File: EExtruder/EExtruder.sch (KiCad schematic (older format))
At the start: 40 parts, among them J1 20A 50V, J11 Conn_01x03_Male, J2 AudioJack4_Ground, U1 STM32F030C8Tx, U2 DCBuck, Y1 8MHz

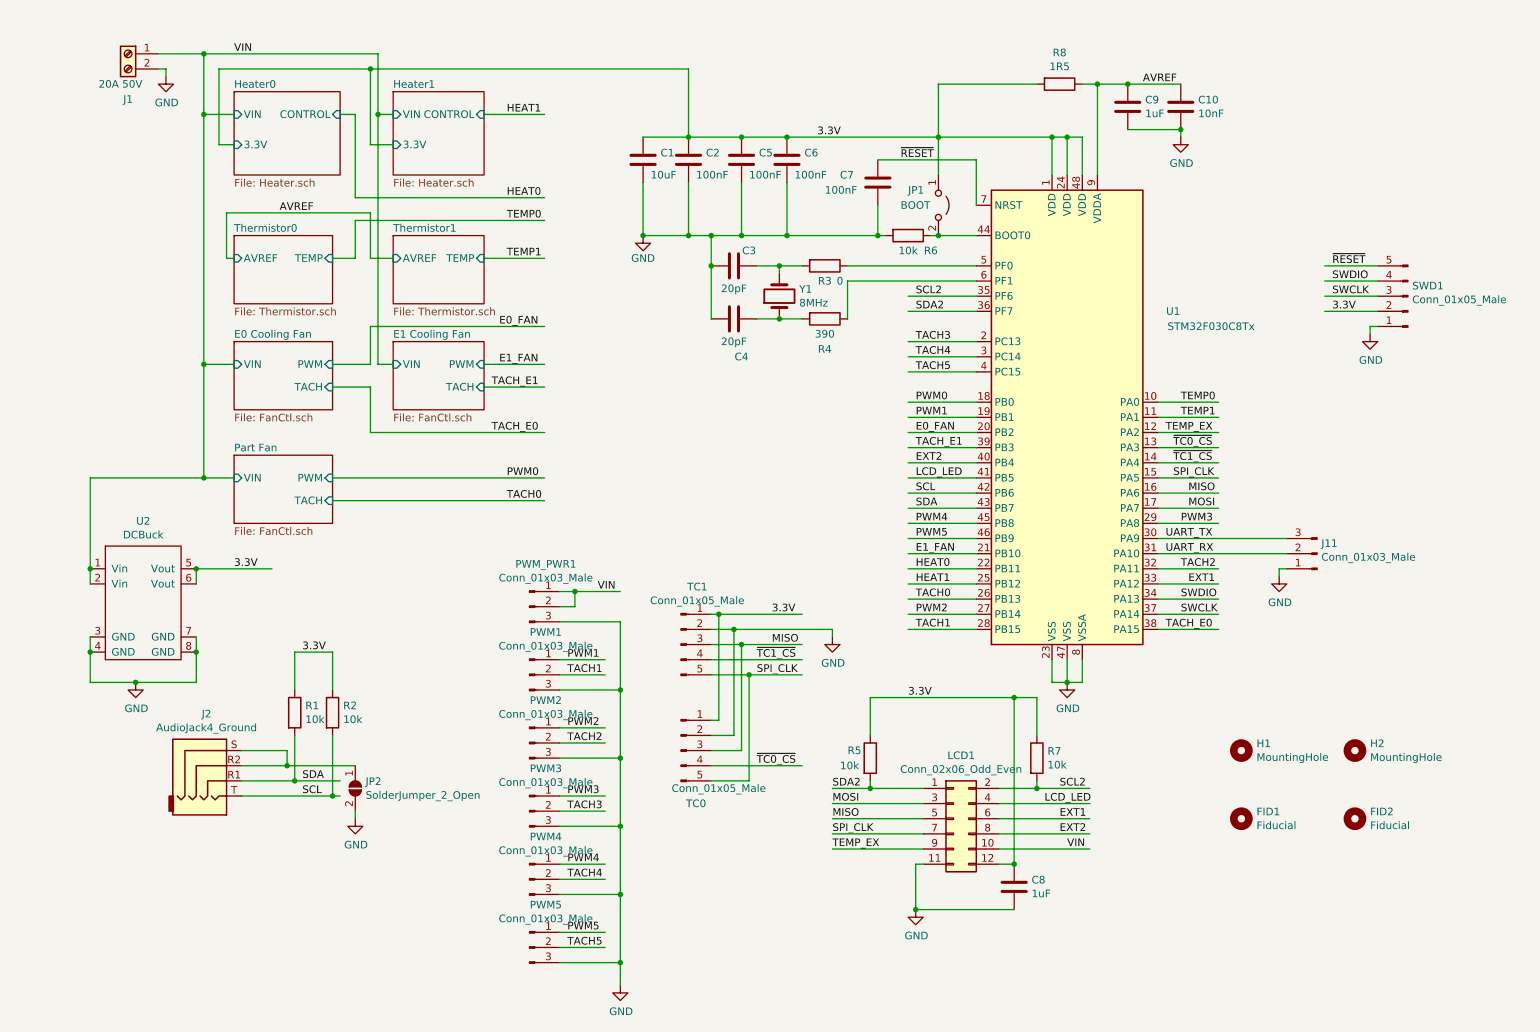
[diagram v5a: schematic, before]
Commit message: Added 3.3V LDO, updated TC connectors to 6 pins. Re-arranged the layout.
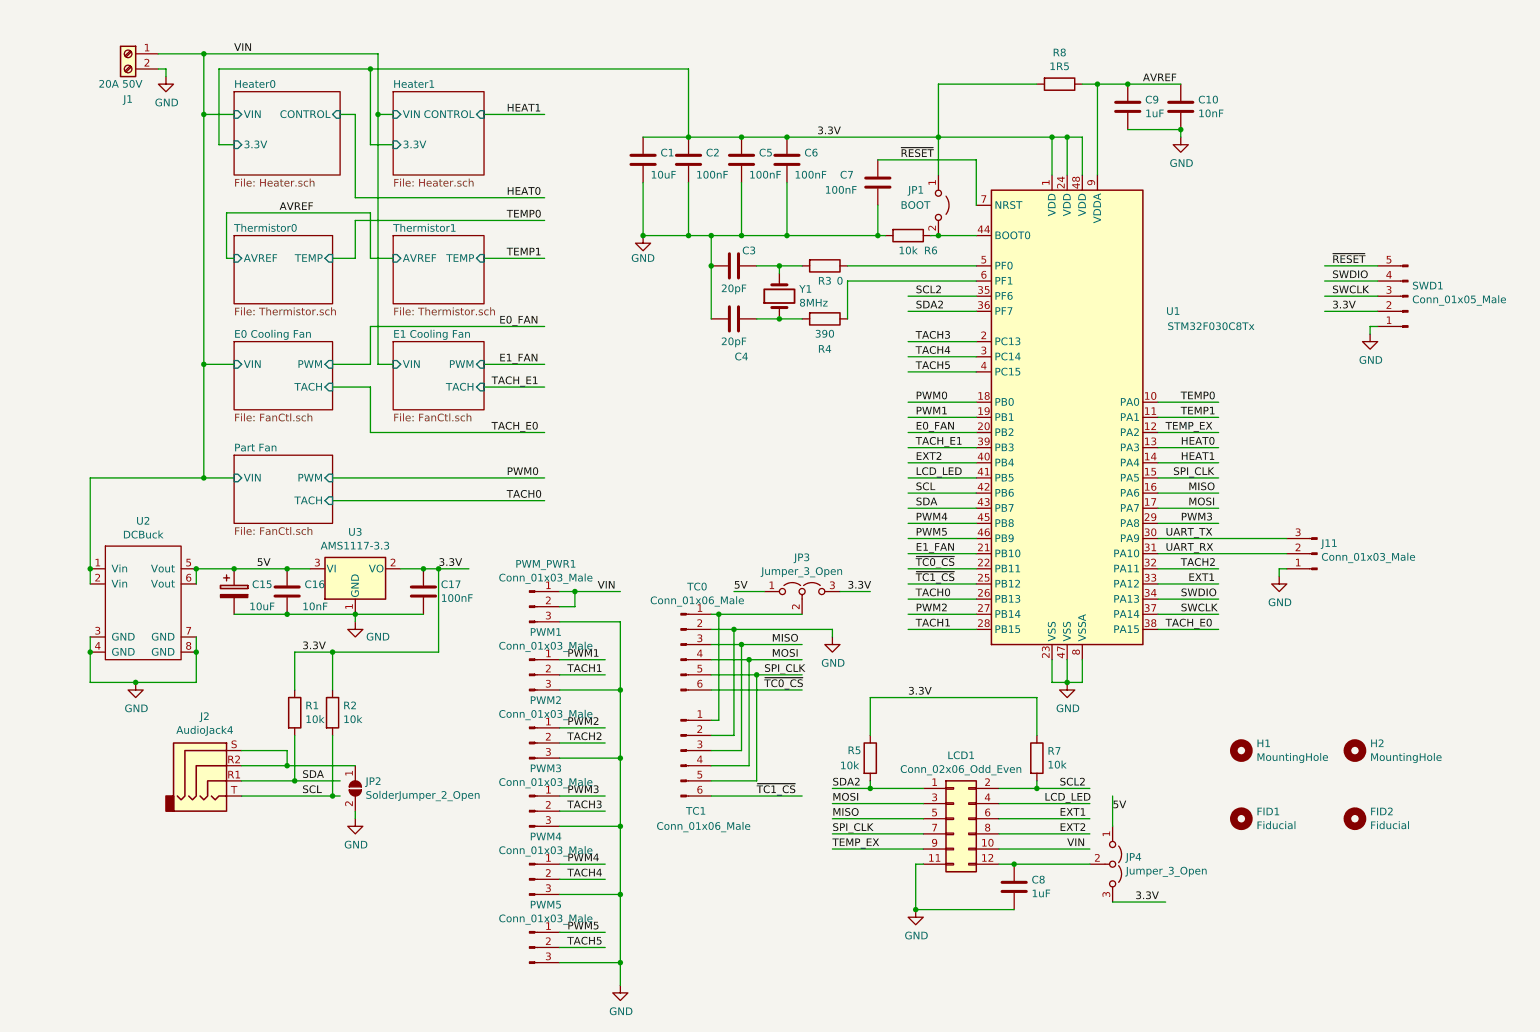
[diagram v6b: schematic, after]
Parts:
- removed J2: AudioJack4_Ground, PJ320D:Jack_3.5mm_PJ320D_Horizontal, symbol Connector:AudioJack4_Ground
- removed TC0, TC1: Conn_01x05_Male, Connector_PinHeader_2.54mm:PinHeader_1x05_P2.54mm_Vertical, symbol Connector:Conn_01x05_Male
- added C15: 10uF, Local:C_0603_1608Metric, symbol Device:CP
- added C16: 10nF, Local:C_0603_1608Metric, symbol Device:C
- added C17: 100nF, Local:C_0603_1608Metric, symbol Device:C
- added J2: AudioJack4, PJ320D:Jack_3.5mm_PJ320D_Horizontal, symbol Connector:AudioJack4
- added JP3, JP4: Jumper_3_Open, Jumper:SolderJumper-3_P1.3mm_Open_Pad1.0x1.5mm, symbol Jumper:Jumper_3_Open
- added TC0, TC1: Conn_01x06_Male, Connector_PinHeader_2.54mm:PinHeader_1x06_P2.54mm_Vertical, symbol Connector:Conn_01x06_Male
- added U3: AMS1117-3.3, Package_TO_SOT_SMD:SOT-223-3_TabPin2, symbol Regulator_Linear:AMS1117-3.3
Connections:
- net labels added: 5V
- wire segments 231 -> 249
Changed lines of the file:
@@
 EESchema Schematic File Version 4
 LIBS:EExtruder-cache
-EELAYER 28 0
+EELAYER 29 0
 EELAYER END
 $Descr A4 11693 8268
@@
 Text Label 8200 3350 0    50   ~ 0
 TEMP_EX
-Text Label 8250 3450 0    50   ~ 0
-~TC0_CS
-Text Label 8250 3550 0    50   ~ 0
-~TC1_CS
 Text Label 8250 3650 0    50   ~ 0
 SPI_CLK
@@
 Text Label 6550 4150 0    50   ~ 0
 E1_FAN
-Text Label 6550 4250 0    50   ~ 0
-HEAT0
-Text Label 6550 4350 0    50   ~ 0
-HEAT1
 Text Label 6550 4450 0    50   ~ 0
 TACH0
@@
 Text Label 2050 850  0    50   ~ 0
 VIN
-$Comp
-L Connector:Conn_01x05_Male TC1
-U 1 1 5BEB14A1
-P 5000 4750
-F 0 "TC1" H 5108 5131 50  0000 C CNN
-F 1 "Conn_01x05_Male" H 5108 5040 50  0000 C CNN
-F 2 "Connector_PinHeader_2.54mm:PinHeader_1x05_P2.54mm_Vertical" H 5000 4750 50  0001 C CNN
-F 3 "~" H 5000 4750 50  0001 C CNN
-	1    5000 4750
-	1    0    0    -1
-$EndComp
-$Comp
-L Connector:Conn_01x05_Male TC0
-U 1 1 5BEB5291
-P 5000 5450
-F 0 "TC0" H 5100 5100 50  0000 C CNN
-F 1 "Conn_01x05_Male" H 5250 5200 50  0000 C CNN
-F 2 "Connector_PinHeader_2.54mm:PinHeader_1x05_P2.54mm_Vertical" H 5000 5450 50  0001 C CNN
-F 3 "~" H 5000 5450 50  0001 C CNN
-	1    5000 5450
-	1    0    0    -1
-$EndComp
-Wire Wire Line
-	5200 5550 5800 5550
-Wire Wire Line
-	5200 4950 5450 4950
 Wire Wire Line
 	5200 4550 5250 4550
@@
 	5200 4750 5400 4750
 Wire Wire Line
-	5200 4850 5800 4850
-Text Label 5600 4550 0    50   ~ 0
-3.3V
+	5200 4850 5450 4850
 Text Label 5600 4750 0    50   ~ 0
 MISO
-Text Label 5500 4850 0    50   ~ 0
-~TC1_CS
-Text Label 5500 4950 0    50   ~ 0
+Text Label 5550 4950 0    50   ~ 0
 SPI_CLK
-Text Label 5500 5550 0    50   ~ 0
-~TC0_CS
-Wire Wire Line
-	5200 5650 5450 5650
-Wire Wire Line
-	5450 5650 5450 4950
-Connection ~ 5450 4950
-Wire Wire Line
-	5450 4950 5800 4950
 Wire Wire Line
 	5200 5450 5400 5450
@@
 	7350 5350 7350 5100
 Wire Wire Line
-	7350 5100 7200 5100
-Wire Wire Line
 	6250 5100 6250 5350
 Text Label 6500 5100 0    50   ~ 0
@@
 Wire Wire Line
 	7100 6000 7700 6000
-Connection ~ 7200 5100
-Wire Wire Line
-	7200 5100 6250 5100
 $Comp
 L power:GND #PWR06
@@
 	7100 6200 7200 6200
 Wire Wire Line
-	7200 5100 7200 6200
-Connection ~ 7200 6200
-Wire Wire Line
 	7200 6500 6550 6500
 Connection ~ 6550 6500
@@
 Connection ~ 1850 3650
 Wire Wire Line
-	1800 4250 2300 4250
-Text Label 2050 4250 0    50   ~ 0
-3.3V
-Wire Wire Line
 	1800 4800 1800 5000
-$Comp
-L Connector:AudioJack4_Ground J2
-U 1 1 5C23C3B0
-P 1900 5550
-F 0 "J2" H 1868 5892 50  0000 C CNN
-F 1 "AudioJack4_Ground" H 1868 5801 50  0000 C CNN
-F 2 "PJ320D:Jack_3.5mm_PJ320D_Horizontal" H 1900 5550 50  0001 C CNN
-F 3 "~" H 1900 5550 50  0001 C CNN
-	1    1900 5550
-	1    0    0    -1
-$EndComp
 $Comp
 L BuckConverter:DCBuck U2
@@
 	1    0    0    -1
 $EndComp
+$Comp
+L Connector:Conn_01x06_Male TC0
+U 1 1 5C3BD554
+P 5000 4750
+F 0 "TC0" H 5108 5131 50  0000 C CNN
+F 1 "Conn_01x06_Male" H 5108 5040 50  0000 C CNN
+F 2 "Connector_PinHeader_2.54mm:PinHeader_1x06_P2.54mm_Vertical" H 5000 4750 50  0001 C CNN
+F 3 "~" H 5000 4750 50  0001 C CNN
+	1    5000 4750
+	1    0    0    -1
+$EndComp
+$Comp
+L Connector:Conn_01x06_Male TC1
+U 1 1 5C3BE824
+P 5000 5450
+F 0 "TC1" H 5100 5050 50  0000 C CNN
+F 1 "Conn_01x06_Male" H 5150 4950 50  0000 C CNN
+F 2 "Connector_PinHeader_2.54mm:PinHeader_1x06_P2.54mm_Vertical" H 5000 5450 50  0001 C CNN
+F 3 "~" H 5000 5450 50  0001 C CNN
+	1    5000 5450
+	1    0    0    -1
+$EndComp
+Wire Wire Line
+	5200 4950 5500 4950
+Wire Wire Line
+	5200 5550 5450 5550
+Wire Wire Line
+	5450 5550 5450 4850
+Connection ~ 5450 4850
+Wire Wire Line
+	5450 4850 5800 4850
+Wire Wire Line
+	5500 5650 5500 4950
+Wire Wire Line
+	5200 5650 5500 5650
+Connection ~ 5500 4950
+Wire Wire Line
+	5500 4950 5800 4950
+Text Label 5600 4850 0    50   ~ 0
+MOSI
+Wire Wire Line
+	5200 5050 5800 5050
+Wire Wire Line
+	5200 5750 5800 5750
+Text Label 5500 5750 0    50   ~ 0
+~TC1_CS
+Text Label 5550 5050 0    50   ~ 0
+~TC0_CS
+$Comp
+L Regulator_Linear:AMS1117-3.3 U3
+U 1 1 5C40648A
+P 2850 4250
+F 0 "U3" H 2850 4492 50  0000 C CNN
+F 1 "AMS1117-3.3" H 2850 4401 50  0000 C CNN
+F 2 "Package_TO_SOT_SMD:SOT-223-3_TabPin2" H 2850 4450 50  0001 C CNN
+F 3 "http://www.advanced-monolithic.com/pdf/ds1117.pdf" H 2950 4000 50  0001 C CNN
+	1    2850 4250
+	1    0    0    -1
+$EndComp
+Wire Wire Line
+	3150 4250 3300 4250
+Text Label 3400 4250 0    50   ~ 0
+3.3V
+$Comp
+L power:GND #PWR018
+U 1 1 5C41A303
+P 2850 4600
+F 0 "#PWR018" H 2850 4350 50  0001 C CNN
+F 1 "GND" H 3000 4500 50  0000 C CNN
+F 2 "" H 2850 4600 50  0001 C CNN
+F 3 "" H 2850 4600 50  0001 C CNN
+	1    2850 4600
+	1    0    0    -1
+$EndComp
+Wire Wire Line
+	2850 4600 2850 4550
+Wire Wire Line
+	1800 4250 2050 4250
+$Comp
+L Device:CP C15
+U 1 1 5C43F401
+P 2050 4400
+F 0 "C15" H 2168 4446 50  0000 L CNN
+F 1 "10uF" H 2150 4300 50  0000 L CNN
+F 2 "Local:C_0603_1608Metric" H 2088 4250 50  0001 C CNN
+F 3 "~" H 2050 4400 50  0001 C CNN
+	1    2050 4400
+	1    0    0    -1
+$EndComp
+Connection ~ 2050 4250
+Wire Wire Line
+	2050 4250 2400 4250
+$Comp
+L Device:C C16
+U 1 1 5C440037
+P 2400 4400
+F 0 "C16" H 2515 4446 50  0000 L CNN
+F 1 "10nF" H 2500 4300 50  0000 L CNN
+F 2 "Local:C_0603_1608Metric" H 2438 4250 50  0001 C CNN
+F 3 "~" H 2400 4400 50  0001 C CNN
+	1    2400 4400
+	1    0    0    -1
+$EndComp
+Connection ~ 2400 4250
+Wire Wire Line
+	2400 4250 2550 4250
+$Comp
+L Device:C C17
+U 1 1 5C4407B0
+P 3300 4400
+F 0 "C17" H 3415 4446 50  0000 L CNN
+F 1 "100nF" H 3415 4355 50  0000 L CNN
+F 2 "Local:C_0603_1608Metric" H 3338 4250 50  0001 C CNN
+F 3 "~" H 3300 4400 50  0001 C CNN
+	1    3300 4400
+	1    0    0    -1
+$EndComp
+Connection ~ 3300 4250
+Wire Wire Line
+	3300 4250 3400 4250
+Wire Wire Line
+	2050 4550 2400 4550
+Connection ~ 2850 4550
+Connection ~ 2400 4550
+Wire Wire Line
+	2400 4550 2850 4550
+Wire Wire Line
+	3300 4550 2850 4550
+Wire Wire Line
+	2700 4800 3400 4800
+Wire Wire Line
+	3400 4800 3400 4250
+Connection ~ 2700 4800
+Connection ~ 3400 4250
+Wire Wire Line
+	3400 4250 3600 4250
+Text Label 2200 4250 0    50   ~ 0
+5V
+$Comp
+L Jumper:Jumper_3_Open JP3
+U 1 1 5C47C278
+P 5800 4400
+F 0 "JP3" H 5800 4624 50  0000 C CNN
+F 1 "Jumper_3_Open" H 5800 4533 50  0000 C CNN
+F 2 "Jumper:SolderJumper-3_P1.3mm_Open_Pad1.0x1.5mm" H 5800 4400 50  0001 C CNN
+F 3 "~" H 5800 4400 50  0001 C CNN
+	1    5800 4400
+	1    0    0    -1
+$EndComp
+Wire Wire Line
+	5550 4400 5350 4400
+Wire Wire Line
+	6050 4400 6250 4400
+Text Label 6100 4400 0    50   ~ 0
+3.3V
+Text Label 5350 4400 0    50   ~ 0
+5V
+Wire Wire Line
+	6250 5100 7350 5100
+$Comp
+L Jumper:Jumper_3_Open JP4
+U 1 1 5C4A66D1
+P 7850 6200
+F 0 "JP4" V 7804 6287 50  0000 L CNN
+F 1 "Jumper_3_Open" V 7895 6287 50  0000 L CNN
+F 2 "Jumper:SolderJumper-3_P1.3mm_Open_Pad1.0x1.5mm" H 7850 6200 50  0001 C CNN
+F 3 "~" H 7850 6200 50  0001 C CNN
+	1    7850 6200
+	0    1    1    0
+$EndComp
+Wire Wire Line
+	7200 6200 7700 6200
+Connection ~ 7200 6200
+Wire Wire Line
+	7850 5950 7850 5750
+Wire Wire Line
+	7850 6450 8200 6450
+Text Label 7850 5850 0    50   ~ 0
+5V
+Text Label 8000 6450 0    50   ~ 0
+3.3V
+Text Label 8300 3450 0    50   ~ 0
+HEAT0
+Text Label 8300 3550 0    50   ~ 0
+HEAT1
+Text Label 6550 4250 0    50   ~ 0
+~TC0_CS
+Text Label 6550 4350 0    50   ~ 0
+~TC1_CS
+$Comp
+L Connector:AudioJack4 J2
+U 1 1 5C503546
+P 1900 5550
+F 0 "J2" H 1857 5875 50  0000 C CNN
+F 1 "AudioJack4" H 1857 5784 50  0000 C CNN
+F 2 "PJ320D:Jack_3.5mm_PJ320D_Horizontal" H 1900 5550 50  0001 C CNN
+F 3 "~" H 1900 5550 50  0001 C CNN
+	1    1900 5550
+	1    0    0    -1
+$EndComp

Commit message: Added voltage selector for the fans.
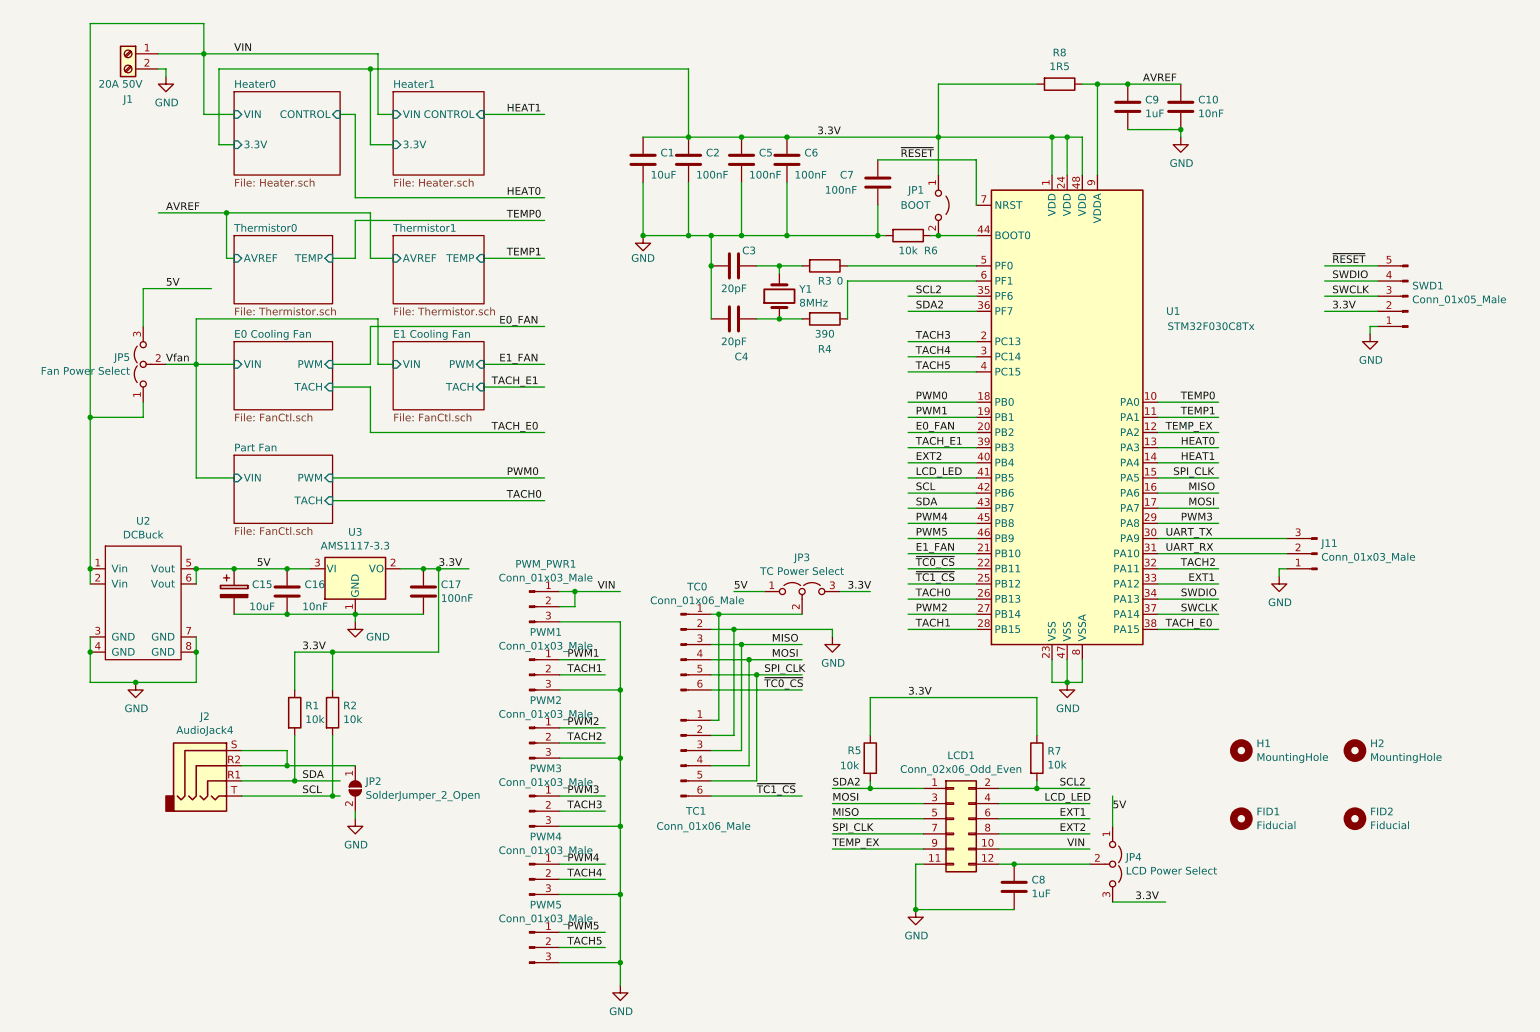
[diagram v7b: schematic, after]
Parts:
- added JP5: Fan Power Select, Connector_PinHeader_2.54mm:PinHeader_1x03_P2.54mm_Vertical, symbol Jumper:Jumper_3_Open
- JP3: value Jumper_3_Open -> TC Power Select
- JP4: value Jumper_3_Open -> LCD Power Select
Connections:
- net labels added: Vfan
- wire segments 249 -> 258
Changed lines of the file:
@@
 	3100 2900 3000 2900
 Wire Wire Line
-	3000 2900 3000 1250
-Wire Wire Line
 	3100 1250 3000 1250
-Connection ~ 3000 1250
 Wire Wire Line
 	3000 1250 3000 850
 Wire Wire Line
-	2050 2900 1850 2900
-Wire Wire Line
-	1850 2900 1850 1250
-Wire Wire Line
 	1850 850  3000 850
 Wire Wire Line
 	2050 1250 1850 1250
-Connection ~ 1850 1250
 Wire Wire Line
 	1850 1250 1850 850
@@
 F4 "TACH" I R 2700 3800 50
 $EndSheet
-Wire Wire Line
-	2050 3650 1850 3650
-Wire Wire Line
-	1850 3650 1850 2900
-Connection ~ 1850 2900
 $Comp
 L MCU_ST_STM32F0:STM32F030C8Tx U1
@@
 Wire Wire Line
 	2950 2200 3100 2200
-Text Label 2350 1900 0    50   ~ 0
+Text Label 1600 1900 0    50   ~ 0
 AVREF
 $Comp
@@
 Connection ~ 1400 5000
 Wire Wire Line
-	1100 4250 1100 3650
-Wire Wire Line
-	1100 3650 1850 3650
-Connection ~ 1850 3650
-Wire Wire Line
 	1800 4800 1800 5000
 $Comp
@@
 P 5800 4400
 F 0 "JP3" H 5800 4624 50  0000 C CNN
-F 1 "Jumper_3_Open" H 5800 4533 50  0000 C CNN
+F 1 "TC Power Select" H 5800 4533 50  0000 C CNN
 F 2 "Jumper:SolderJumper-3_P1.3mm_Open_Pad1.0x1.5mm" H 5800 4400 50  0001 C CNN
 F 3 "~" H 5800 4400 50  0001 C CNN
@@
 P 7850 6200
 F 0 "JP4" V 7804 6287 50  0000 L CNN
-F 1 "Jumper_3_Open" V 7895 6287 50  0000 L CNN
+F 1 "LCD Power Select" V 7895 6287 50  0000 L CNN
 F 2 "Jumper:SolderJumper-3_P1.3mm_Open_Pad1.0x1.5mm" H 7850 6200 50  0001 C CNN
 F 3 "~" H 7850 6200 50  0001 C CNN
@@
 	1    0    0    -1
 $EndComp
+Wire Wire Line
+	2000 1900 1550 1900
+Connection ~ 2000 1900
+Wire Wire Line
+	1100 650  1850 650
+Wire Wire Line
+	1850 650  1850 850
+Wire Wire Line
+	1100 650  1100 3250
+$Comp
+L Jumper:Jumper_3_Open JP5
+U 1 1 5C51FB51
+P 1450 2900
+F 0 "JP5" V 1496 2987 50  0000 L CNN
+F 1 "Fan Power Select" V 1405 2987 50  0000 L CNN
+F 2 "Connector_PinHeader_2.54mm:PinHeader_1x03_P2.54mm_Vertical" H 1450 2900 50  0001 C CNN
+F 3 "~" H 1450 2900 50  0001 C CNN
+	1    1450 2900
+	0    -1   -1   0
+$EndComp
+Wire Wire Line
+	3000 2900 3000 2600
+Wire Wire Line
+	3000 2600 1800 2600
+Wire Wire Line
+	1800 2600 1800 2900
+Wire Wire Line
+	1800 2900 1600 2900
+Wire Wire Line
+	2050 2900 1800 2900
+Connection ~ 1800 2900
+Wire Wire Line
+	2050 3650 1800 3650
+Wire Wire Line
+	1800 3650 1800 2900
+Wire Wire Line
+	1450 3150 1450 3250
+Wire Wire Line
+	1450 3250 1100 3250
+Connection ~ 1100 3250
+Wire Wire Line
+	1100 3250 1100 4250
+Wire Wire Line
+	1450 2650 1450 2400
+Wire Wire Line
+	1450 2400 1900 2400
+Text Label 1600 2400 0    50   ~ 0
+5V
+Text Label 1600 2900 0    50   ~ 0
+Vfan
 $EndSCHEMATC
